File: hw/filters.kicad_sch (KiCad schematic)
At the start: 37 parts, among them U301 AS183-92LF, U302 AS183-92LF, U303 AS183-92LF, U304 AS183-92LF, U305 AS183-92LF, U306 AS183-92LF, U307 AS183-92LF, U308 AS183-92LF, U309 SN74LVC2G14DCKRE4

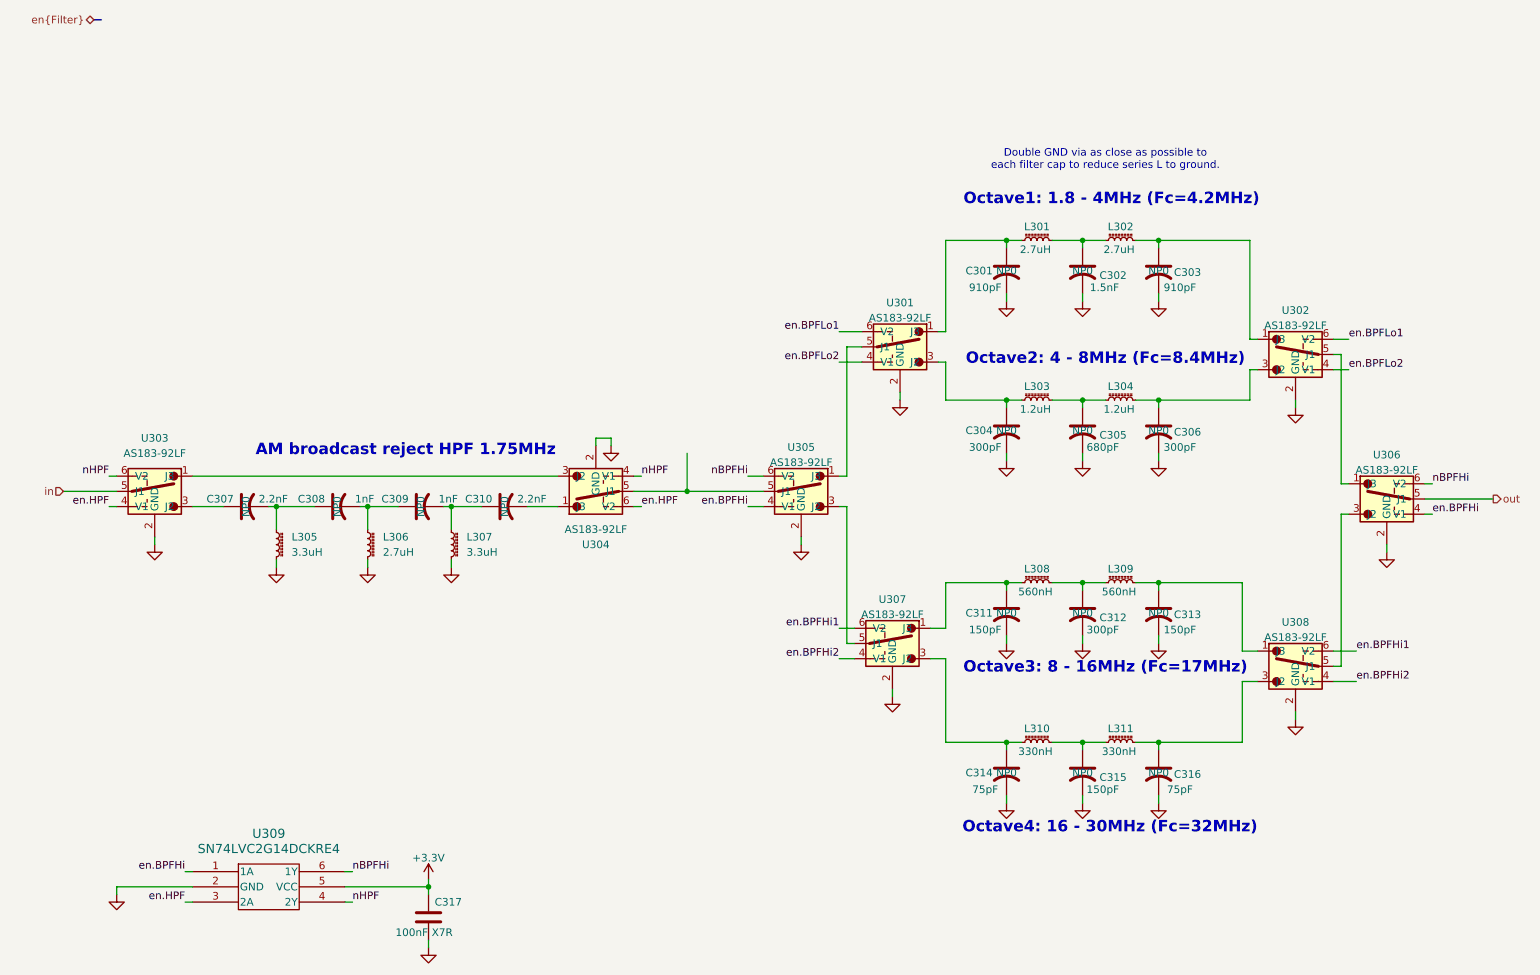
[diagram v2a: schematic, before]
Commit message: Use SP4T GaAsFET switches for BPFs
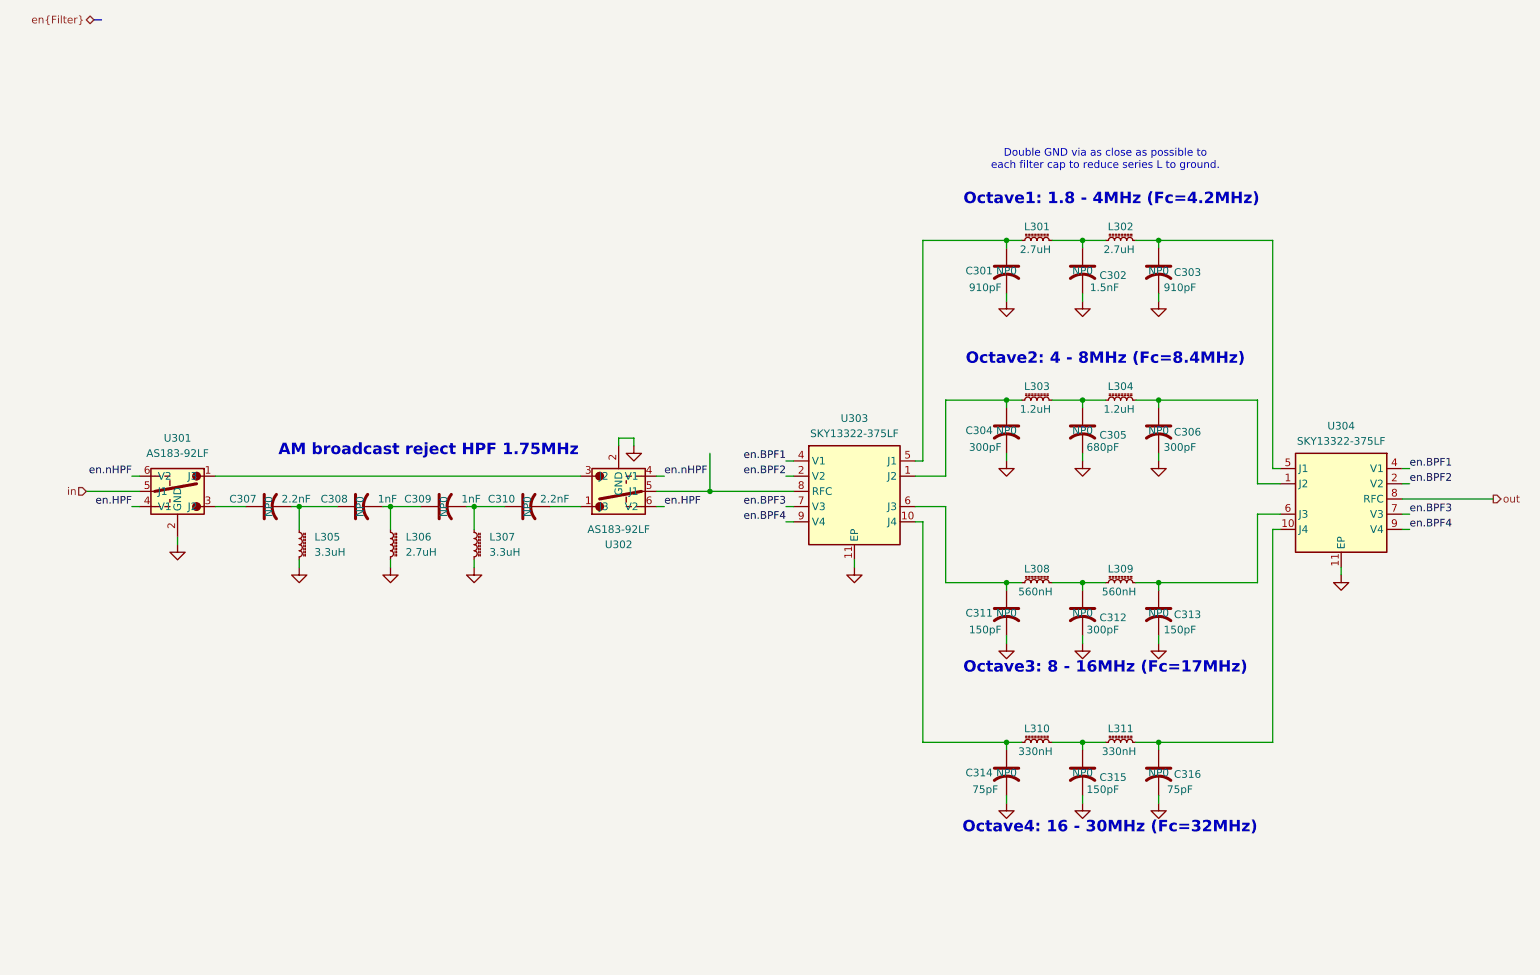
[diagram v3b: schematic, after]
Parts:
- removed C317: 100nF, Capacitor_SMD:C_0402_1005Metric, symbol Device:C
- removed U301, U302, U305, U306, U307, U308: AS183-92LF, Library:SOT65P220X110-6N, symbol Library:AS183-92LF
- removed U309: SN74LVC2G14DCKRE4, Library:SOIC_G14DCK3_TEX, symbol Library:SN74LVC2G14DCK3
- added U303, U304: SKY13322-375LF, Library:SON50P200X300X50-11N-D, symbol Library:SKY13322-375LF
- renumbered U303 to U301, U304 to U302
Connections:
- net GND: now also U303.11 (EP), U304.11 (EP)
- net out: now also U304.8 (RFC)
- net at C311.1, L308.1: now also U303.6 (J3)
- net at C314.1, L310.1: now also U303.10 (J4)
- net at C301.1, L301.1: now also U303.5 (J1)
- net at C304.1, L303.1: now also U303.1 (J2)
- net at U302.5 (J1): now also U303.8 (RFC)
- net at C303.1, L302.2: now also U304.5 (J1)
- net at C306.1, L304.2: now also U304.1 (J2)
- net at C313.1, L309.2: now also U304.6 (J3)
- net at C316.1, L311.2: now also U304.10 (J4)
- net nHPF renamed en.nHPF
- new net en.BPF1: U303.4 (V1), U304.4 (V1)
- new net en.BPF2: U303.2 (V2), U304.2 (V2)
- new net en.BPF3: U303.7 (V3), U304.7 (V3)
- new net en.BPF4: U303.9 (V4), U304.9 (V4)
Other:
- moved on the sheet: C307, C308, C309, C310, L305, L306, L307, U301, U302

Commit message: DVT4 uses higher Q inductors, some layout tweaks, series R on SWDCLK and SWDIO.
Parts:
- L310, L311: footprint Library:L_1008_2520Metric_Pad1.43x2.20mm_HandSolder-keepout -> Inductor_SMD:L_Coilcraft_2929SQ-331; symbol Device:L_Ferrite_Small -> Device:L_Small; MPN 1008CS-331XJR -> 2929SQ-331JEC; Mouser Part Number 994-1008CS-331XJRC -> (none); Mouser_PN 994-1008CS-331XJRC -> (none)
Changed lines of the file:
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@@
 	)
 	(symbol
-		(lib_id "Device:L_Ferrite_Small")
+		(lib_id "Device:L_Small")
 		(at 195.58 137.16 90)
 		(unit 1)
@@
 			)
 		)
-		(property "Footprint" "Library:L_1008_2520Metric_Pad1.43x2.20mm_HandSolder-keepout"
+		(property "Footprint" "Inductor_SMD:L_Coilcraft_2929SQ-331"
 			(at 195.58 137.16 0)
 			(effects
@@
 			)
 		)
-		(property "Description" "SMD RF chip inductor, 330nH, 1008"
+		(property "Description" "Inductor, small symbol"
 			(at 195.58 137.16 0)
 			(effects
@@
 			)
 		)
-		(property "Mouser Part Number" "994-1008CS-331XJRC"
+		(property "Mouser Part Number" ""
 			(at 195.58 137.16 90)
 			(effects
@@
 			)
 		)
-		(property "MPN" "1008CS-331XJR"
+		(property "MPN" "2929SQ-331JEC"
 			(at 195.58 137.16 90)
 			(effects
@@
 			)
 		)
-		(property "Mouser_PN" "994-1008CS-331XJRC"
+		(property "Mouser_PN" ""
 			(at 195.58 137.16 90)
 			(effects
@@
 	)
 	(symbol
-		(lib_id "Device:L_Ferrite_Small")
+		(lib_id "Device:L_Small")
 		(at 181.61 137.16 90)
 		(unit 1)
@@
 			)
 		)
-		(property "Footprint" "Library:L_1008_2520Metric_Pad1.43x2.20mm_HandSolder-keepout"
+		(property "Footprint" "Inductor_SMD:L_Coilcraft_2929SQ-331"
 			(at 181.61 137.16 0)
 			(effects
@@
 			)
 		)
-		(property "Description" "SMD RF chip inductor, 330nH, 1008"
+		(property "Description" "Inductor, small symbol"
 			(at 181.61 137.16 0)
 			(effects
@@
 			)
 		)
-		(property "Mouser Part Number" "994-1008CS-331XJRC"
+		(property "Mouser Part Number" ""
 			(at 181.61 137.16 90)
 			(effects
@@
 			)
 		)
-		(property "MPN" "1008CS-331XJR"
+		(property "MPN" "2929SQ-331JEC"
 			(at 181.61 137.16 90)
 			(effects
@@
 			)
 		)
-		(property "Mouser_PN" "994-1008CS-331XJRC"
+		(property "Mouser_PN" ""
 			(at 181.61 137.16 90)
 			(effects

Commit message: DVT4 seems ready to quote with JCLPCB part numbers.
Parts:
- C301, C303: LCSC_PN (none) -> C458911
- C302: LCSC_PN (none) -> C668348
- C304, C306, C312: LCSC_PN (none) -> C126505
- C305: LCSC_PN (none) -> C113781
- C307, C310: LCSC_PN (none) -> C2167434
- C308, C309: LCSC_PN (none) -> C53547
- C311, C313, C315: LCSC_PN (none) -> C12220
- C314, C316: LCSC_PN (none) -> C37809
- L301, L302, L306: LCSC_PN (none) -> C20882986
- L303, L304: LCSC_PN (none) -> C52259879
- L305, L307: LCSC_PN (none) -> C49241336
- L308, L309: LCSC_PN (none) -> C54534441
- L310, L311: LCSC_PN (none) -> C19271242
- U303, U304: LCSC_PN (none) -> C151465

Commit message: DVT5 or whatever follows DVT testing WIP
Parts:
- L301, L302, L303, L304, L305, L306, L307: footprint Library:L_1812_4532Metric-keepout -> Inductor_SMD:L_1812_4532Metric
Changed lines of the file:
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@@
 			)
 		)
-		(property "Footprint" "Library:L_1812_4532Metric-keepout"
+		(property "Footprint" "Inductor_SMD:L_1812_4532Metric"
 			(at 181.61 53.34 0)
 			(effects
@@
 			)
 		)
-		(property "Footprint" "Library:L_1812_4532Metric-keepout"
+		(property "Footprint" "Inductor_SMD:L_1812_4532Metric"
 			(at 181.61 80.01 0)
 			(effects
@@
 			)
 		)
-		(property "Footprint" "Library:L_1812_4532Metric-keepout"
+		(property "Footprint" "Inductor_SMD:L_1812_4532Metric"
 			(at 195.58 53.34 0)
 			(effects
@@
 			)
 		)
-		(property "Footprint" "Library:L_1812_4532Metric-keepout"
+		(property "Footprint" "Inductor_SMD:L_1812_4532Metric"
 			(at 73.66 104.14 0)
 			(effects
@@
 			)
 		)
-		(property "Footprint" "Library:L_1812_4532Metric-keepout"
+		(property "Footprint" "Inductor_SMD:L_1812_4532Metric"
 			(at 87.63 104.14 0)
 			(effects
@@
 			)
 		)
-		(property "Footprint" "Library:L_1812_4532Metric-keepout"
+		(property "Footprint" "Inductor_SMD:L_1812_4532Metric"
 			(at 195.58 80.01 0)
 			(effects
@@
 			)
 		)
-		(property "Footprint" "Library:L_1812_4532Metric-keepout"
+		(property "Footprint" "Inductor_SMD:L_1812_4532Metric"
 			(at 58.42 104.14 0)
 			(effects

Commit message: Close to being able to build again with displays as shields. Driver is there but not building yet, main still needs some work too.
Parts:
- L310, L311: LCSC_PN C19271242 -> C20623511
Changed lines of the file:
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@@
 			)
 		)
-		(property "LCSC_PN" "C19271242"
+		(property "LCSC_PN" "C20623511"
 			(at 195.58 137.16 90)
 			(effects
@@
 			)
 		)
-		(property "LCSC_PN" "C19271242"
-			(at 181.61 137.16 90)
-			(effects
+		(property "LCSC_PN" "C20623511"
+			(at 181.61 137.16 90)
+			(effects
